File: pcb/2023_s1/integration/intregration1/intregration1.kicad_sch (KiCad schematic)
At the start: 42 parts, among them J1 Screw_Terminal_01x02, Q1 2N2219, Q2 2N2219, Q3 2N2219, Q4 2N2219, U1 NRF24L01_Breakout

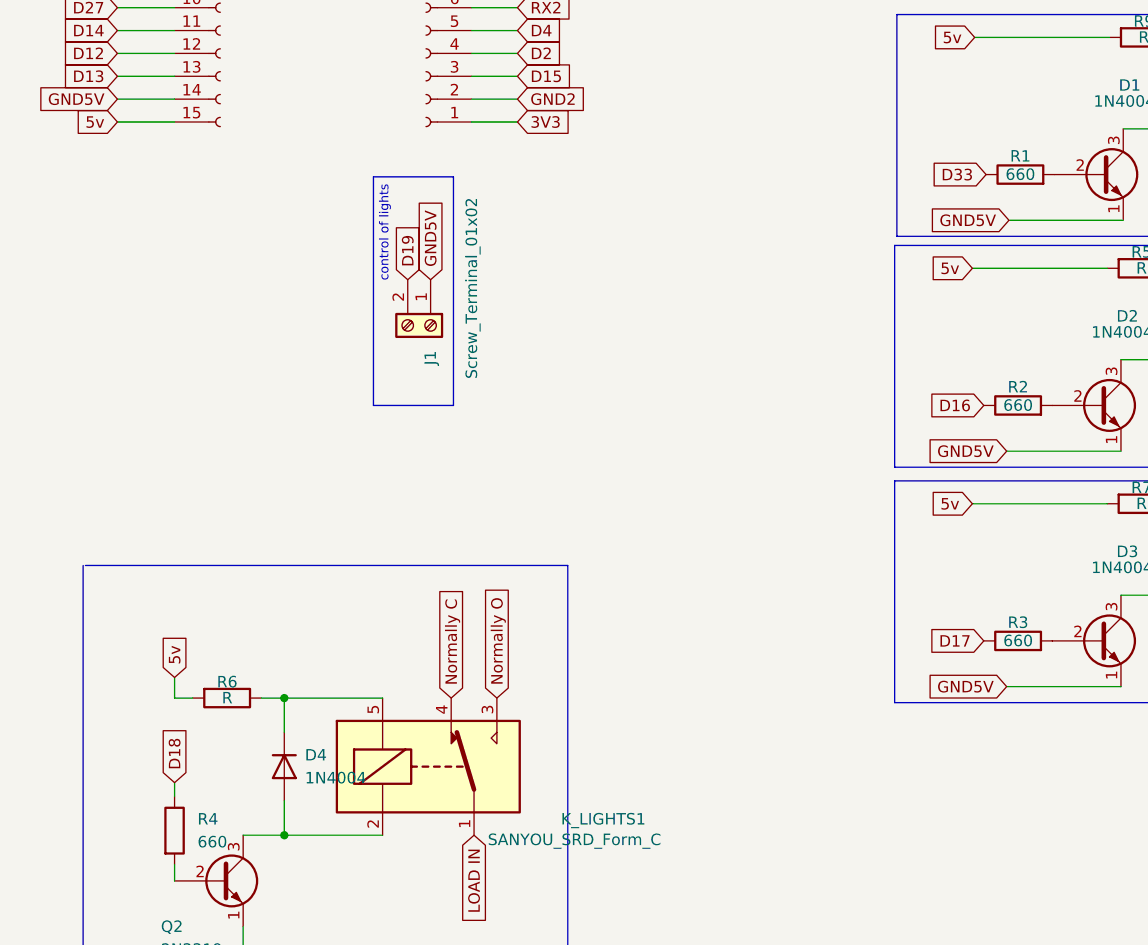
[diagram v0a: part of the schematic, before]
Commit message: update, routed the integration PCB, only production and testing is remaining
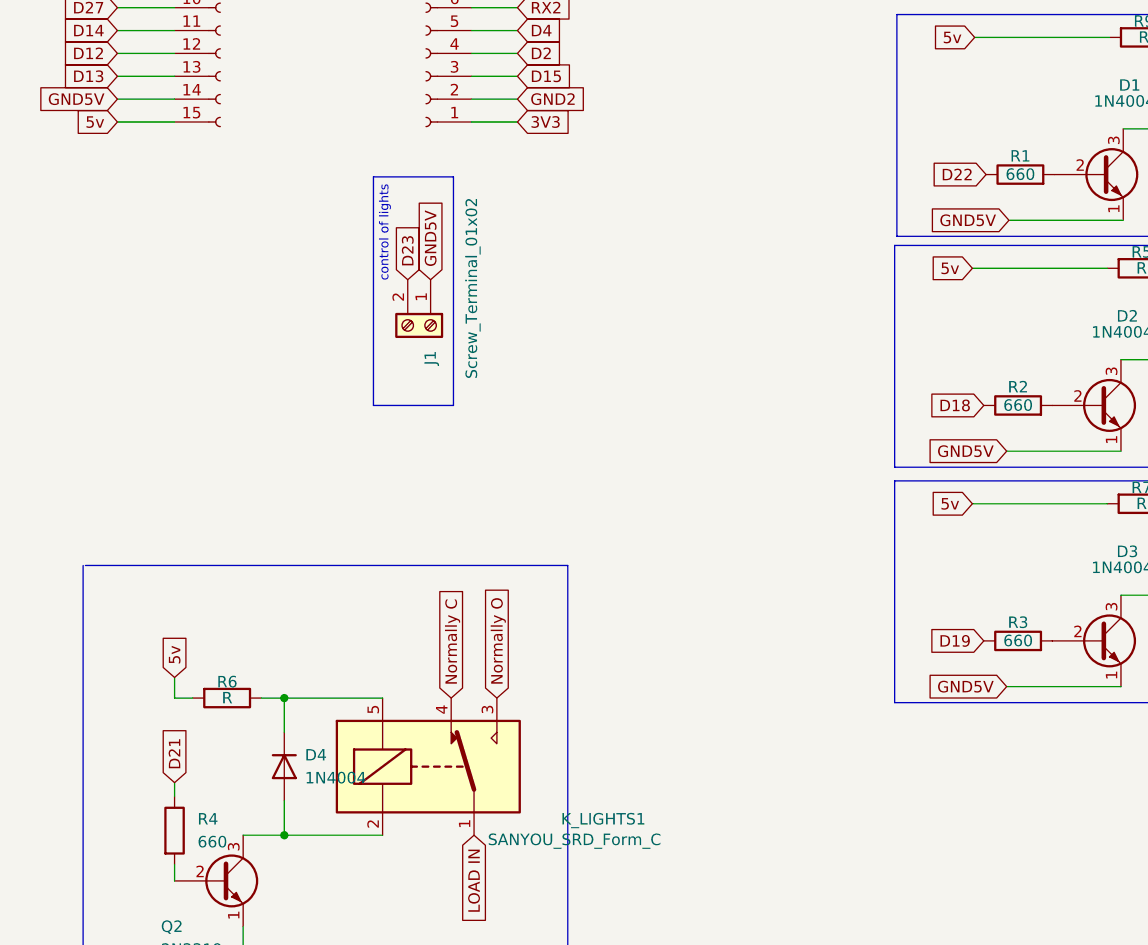
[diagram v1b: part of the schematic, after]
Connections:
- net D16 is gone; now on net D18: R2.1
- net D17 is gone; now on net D19: R3.1
- net D18: no longer R4.1
- net D19: no longer J1.2 (Pin_2)
- net D21: now also R4.1
- net D22: now also R1.1
- net D23: now also J1.2 (Pin_2)
- net D33: no longer R1.1
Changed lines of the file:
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@@
     )
   )
-  (global_label "D18" (shape input) (at 112.522 164.592 90) (fields_autoplaced)
+  (global_label "D21" (shape input) (at 112.522 164.592 90) (fields_autoplaced)
     (effects (font (size 1.27 1.27)) (justify left))
     (property "Intersheetrefs" "${INTERSHEET_REFS}" (at 112.522 157.9972 90)
@@
     )
   )
-  (global_label "D19" (shape input) (at 138.43 108.712 90) (fields_autoplaced)
+  (global_label "D23" (shape input) (at 138.43 108.712 90) (fields_autoplaced)
     (effects (font (size 1.27 1.27)) (justify left))
     (property "Intersheetrefs" "${INTERSHEET_REFS}" (at 138.43 102.1172 90)
@@
     )
   )
-  (global_label "D17" (shape input) (at 202.438 148.844 180) (fields_autoplaced)
+  (global_label "D19" (shape input) (at 202.438 148.844 180) (fields_autoplaced)
     (effects (font (size 1.27 1.27)) (justify right))
     (property "Intersheetrefs" "${INTERSHEET_REFS}" (at 195.8432 148.844 0)
@@
     )
   )
-  (global_label "D33" (shape input) (at 202.692 97.028 180) (fields_autoplaced)
+  (global_label "D22" (shape input) (at 202.692 97.028 180) (fields_autoplaced)
     (effects (font (size 1.27 1.27)) (justify right))
-    (property "Intersheetrefs" "${INTERSHEET_REFS}" (at 196.5899 97.1074 0)
+    (property "Intersheetrefs" "${INTERSHEET_REFS}" (at 196.0972 97.028 0)
       (effects (font (size 1.27 1.27)) (justify right) hide)
     )
@@
     )
   )
-  (global_label "D16" (shape input) (at 202.438 122.682 180) (fields_autoplaced)
+  (global_label "D18" (shape input) (at 202.438 122.682 180) (fields_autoplaced)
     (effects (font (size 1.27 1.27)) (justify right))
     (property "Intersheetrefs" "${INTERSHEET_REFS}" (at 195.8432 122.682 0)
